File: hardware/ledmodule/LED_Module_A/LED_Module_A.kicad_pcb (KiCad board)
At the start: 2 copper layers, 214.1 x 70.5 mm, 140 parts, among them J1 To MAIN_MOD, U1 DS18B20U

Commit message: Preparation for fabrication
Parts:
- added ?: , LOGO, F.Cu at (249.1, 110.9)
- added H1: MountingHole, MountingHole:MountingHole_3.2mm_M3, F.Cu at (60.0, 125.0)
- added H2: MountingHole, MountingHole:MountingHole_3.2mm_M3, F.Cu at (190.0, 125.0)
- added H3: MountingHole, MountingHole:MountingHole_3.2mm_M3, F.Cu at (250.0, 125.0)
- added H4: MountingHole, MountingHole:MountingHole_3.2mm_M3, F.Cu at (250.0, 87.6)
- added H5: MountingHole, MountingHole:MountingHole_3.2mm_M3, F.Cu at (190.0, 100.0)
- added H6: MountingHole, MountingHole:MountingHole_3.2mm_M3, F.Cu at (85.0, 100.0)
- added H7: MountingHole, MountingHole:MountingHole_3.2mm_M3, F.Cu at (47.4, 88.0)
- D_R1, D_R2, D_R3, D_R4, D_R5, D_R6, D_R7, D_R8: value Photo Red -> Red
- moved D_R5 6.18 mm to (90.0, 104.1)
- moved R_A7 4.64 mm to (79.0, 97.3)
- moved D_A9 2.03 mm to (90.9, 96.5)
- moved D_R7 1.86 mm to (190.5, 106.0)
- moved R_B3 1.68 mm to (212.5, 66.0)
- moved R_B2 1.46 mm to (149.9, 67.5)
- moved D_A4 1.38 mm to (149.9, 72.5)
- moved D_B2 0.46 mm to (96.5, 66.5)
- moved D_P5 0.33 mm to (58.8, 104.1)
- moved R_B1 0.33 mm to (53.9, 100.3)
- moved R_B4 0.33 mm to (53.9, 103.9)
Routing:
- net Net-(D_R5-K): track 2.75 -> 15.1 mm
- net Net-(D_A9-K): track 2.49 -> 10.2 mm
- net Net-(D_P6-K): track 23.2 -> 17.0 mm
- net Net-(D_A8-A): track 20.9 -> 16.1 mm
- net /LED_CW: track 111.8 -> 115.7 mm
- net Net-(D_B5-A): track 20.3 -> 22.5 mm
- net Net-(D_B6-K): track 5.31 -> 3.63 mm
- net Net-(D_W4-K): track 19.3 -> 20.5 mm
- net Net-(D_C10-K): track 19.2 -> 20.2 mm
- net Net-(D_A9-A): track 22.3 -> 21.4 mm
- net Net-(D_P8-K): track 25.7 -> 26.5 mm
- net Net-(D_P7-A): track 25.7 -> 26.5 mm
- net Net-(D_W1-A): track 21.3 -> 22.0 mm
- net Net-(D_W6-K): track 23.8 -> 23.1 mm
- net Net-(D_W5-A): track 3.50 -> 4.24 mm
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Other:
- board size 214.1 x 70.5 mm -> 214.6 x 70.5 mm
- board text added: "J1 (back)"
- board text added: "LED Module A v1.0"
- board text added: "WayWayWay"
- board text added: "https://lenaschimmel.de/besteLampe!"

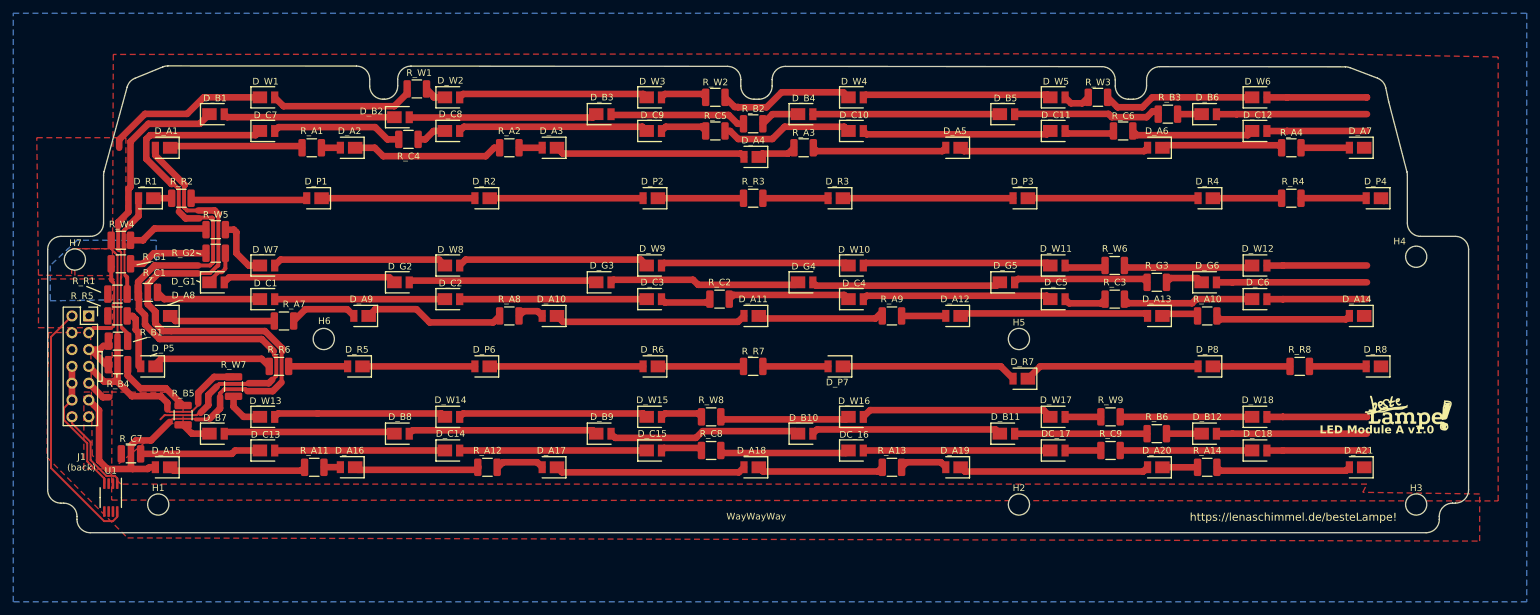
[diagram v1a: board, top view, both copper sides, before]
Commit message: Ready for production - but needs expensive hole plating.
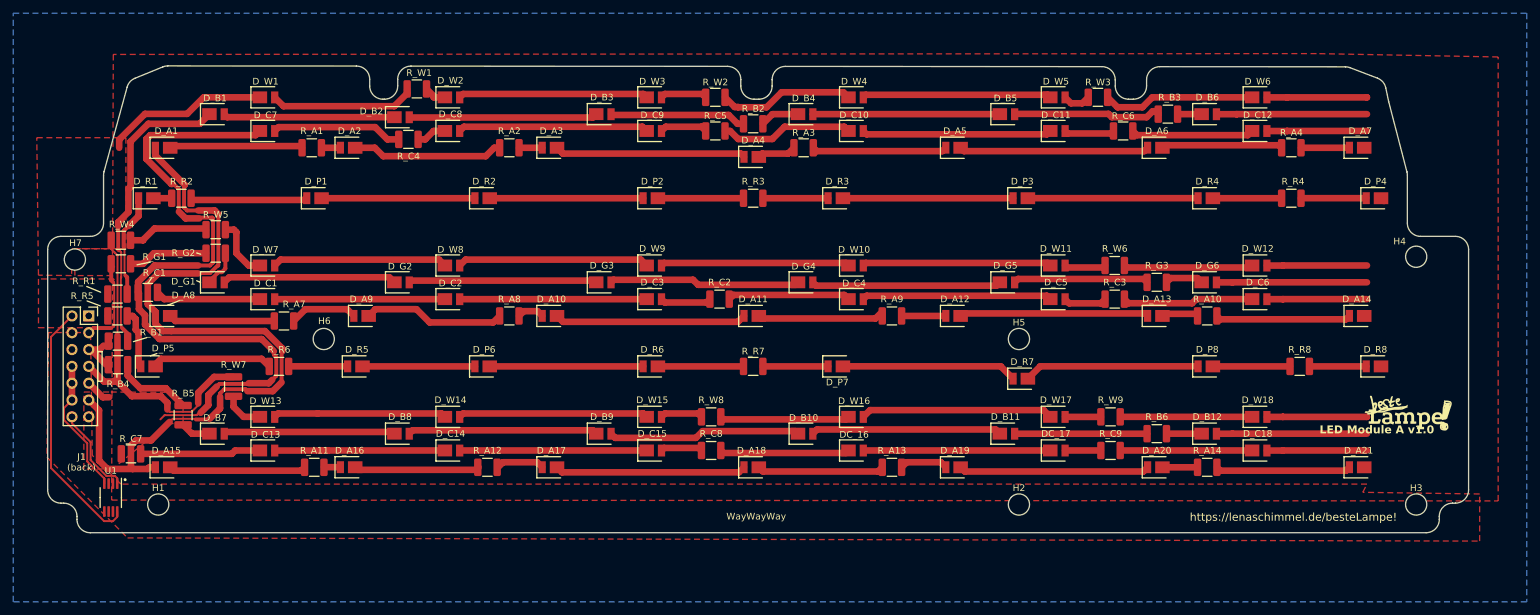
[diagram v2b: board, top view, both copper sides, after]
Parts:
- D_A1, D_A10, D_A11, D_A12, D_A13, D_A14, D_A15, D_A16, D_A17, D_A18, D_A19, D_A2, D_A20, D_A21, D_A3, D_A4, D_A5, D_A6, D_A7, D_A8, D_A9, D_P1, D_P2, D_P3, D_P4, D_P5, D_P6, D_P7, D_P8, D_R1, D_R2, D_R3, D_R4, D_R5, D_R6, D_R7, D_R8: footprint LED_SMD:LED_2835_CREE_JSE28L3E5 -> LED_SMD:LED_2835_CREE_JSE28L3E5_Big_Anode
- J1: value To MAIN_MOD -> Do Not Place
- R_A1, R_A11, R_A7: value 2R2 -> 2.2 Ohm, 0,33W, 5%, 1210 package
- R_A10, R_A12, R_A13, R_A14, R_A2, R_A3, R_A4, R_A8, R_A9, R_C1, R_C2, R_C3, R_C4, R_C5, R_C6, R_C7, R_C8, R_C9, R_G1, R_G2, R_G3, R_W1, R_W2, R_W3, R_W4, R_W5, R_W6, R_W7, R_W8, R_W9: value 18 -> 18 Ohm, 0,5W, 1%, 1210 package
- R_B1, R_B2, R_B3, R_B4, R_B5, R_B6, R_R2, R_R3, R_R4, R_R6, R_R7, R_R8: value 15 -> 15 Ohm, 0,5W, 1%, 1210 package
- R_R1, R_R5: value 4R7 -> 4.7 Ohm, 0,33W, 5%, 1210 package
- U1: value DS18B20U -> DS18B20U+
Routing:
- removed copper zone on B.Cu, net Net-(D_G1-K)

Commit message: SMD pin headers with 90deg rotation
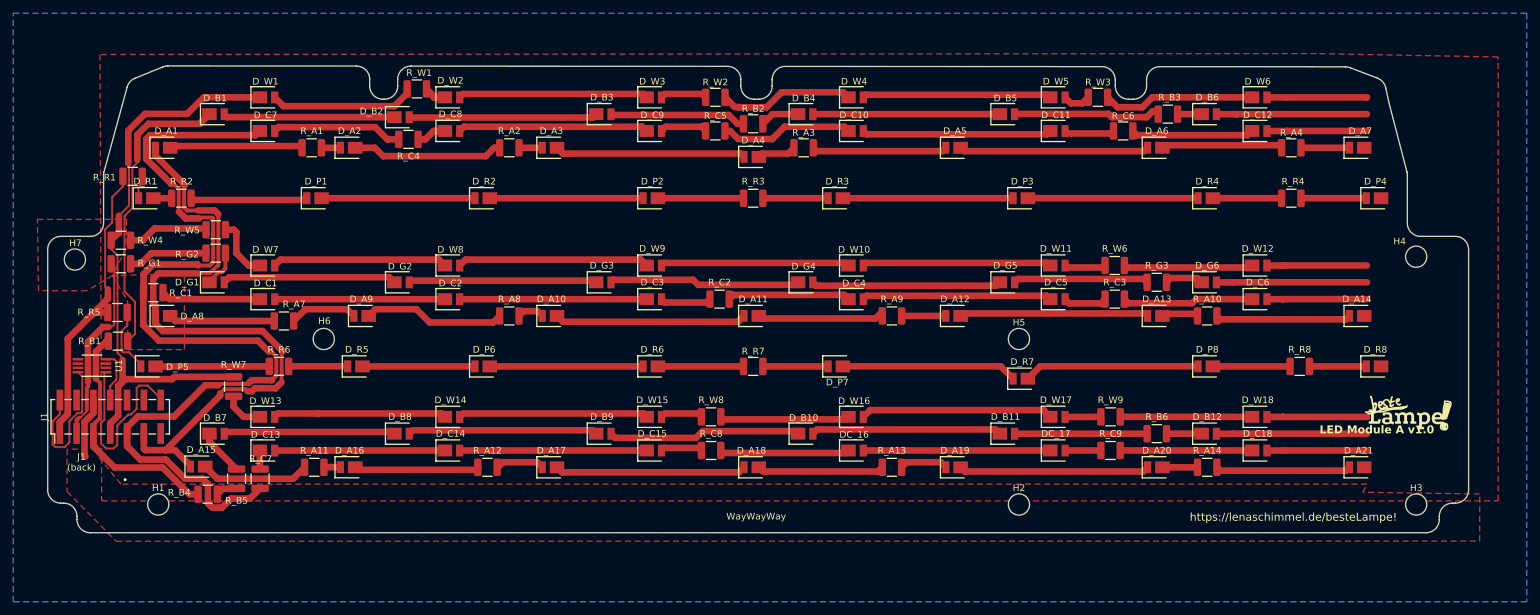
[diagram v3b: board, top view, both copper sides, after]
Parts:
- J1: value Do Not Place -> ~; footprint Connector_PinHeader_2.54mm:PinHeader_2x07_P2.54mm_Vertical_Boxed -> Connector_PinHeader_2.54mm:PinHeader_2x07_P2.54mm_Vertical_SMD; moved to F.Cu
- moved R_B4 23.8 mm to (67.5, 123.4)
- moved U1 20.1 mm to (50.0, 104.0), turned to 180 degrees
- moved R_C7 19.9 mm to (75.4, 121.1), turned to 90 degrees
- moved R_R1 17.9 mm to (56.1, 75.4)
- moved R_B5 12.5 mm to (71.8, 121.1), turned to 90 degrees
- moved J1 8.84 mm to (52.8, 111.8), turned to 90 degrees
- moved D_A15 5.28 mm to (66.2, 119.3)
- moved R_C1 0.83 mm to (59.2, 93.0)
- moved R_R5 0.52 mm to (53.8, 96.0)
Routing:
- net /LED_R: track 0.01 -> 45.9 mm
- net /LED_CW: track 115.7 -> 146.7 mm
- net /LED_B: track 6.06 -> 35.8 mm
- net /LED_A: track 120.8 -> 102.0 mm
- net +3V3: track 38.7 -> 22.1 mm
- net /LED_G: track 14.3 -> 30.3 mm
- net Net-(D_R1-K): track 18.1 -> 2.66 mm
- net Net-(D_C13-K): track 18.2 -> 2.82 mm
- net /TEMP: track 13.7 -> 28.9 mm
- net /LED_WW: track 76.8 -> 90.4 mm
- net GND: track 20.7 -> 7.94 mm
- net +24V: track 159.6 -> 170.0 mm
- net Net-(R_B4-Pad2): track 11.9 -> 3.27 mm
- net Net-(D_A15-A): track 20.7 -> 16.6 mm
- net Net-(D_B7-K): track 4.53 -> 7.49 mm
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- removed copper zone on F.Cu, net /LED_CW
- removed copper zone on F.Cu, net /LED_G

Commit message: New layout with angled SMD header, but probably not aligned correctly.
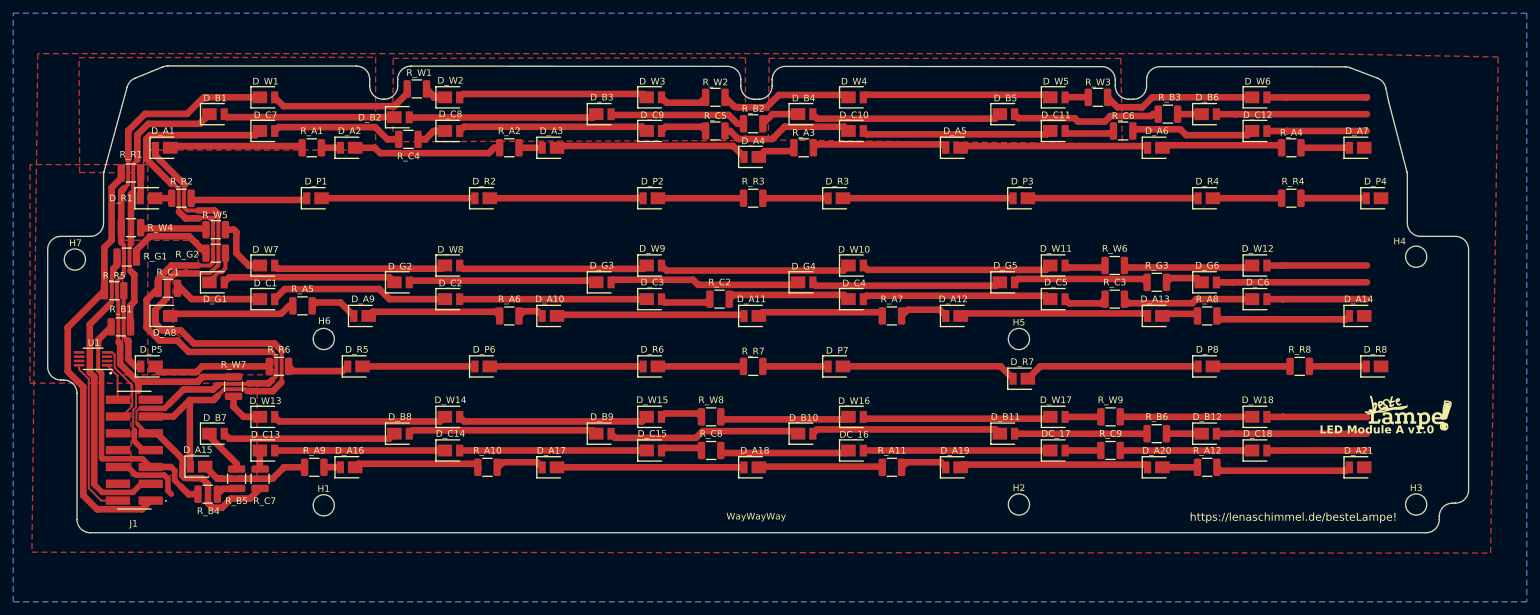
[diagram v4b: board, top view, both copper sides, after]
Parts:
- J1: footprint Connector_PinHeader_2.54mm:PinHeader_2x07_P2.54mm_Vertical_SMD -> TSM:TSM-107-YY-ZZZ-DV-P-TR
- moved H1 25.0 mm to (85.0, 125.1)
- moved J1 6.22 mm to (56.4, 116.8), turned to -90 degrees
- moved R_A5 3.61 mm to (81.8, 95.0)
- moved R_R5 3.33 mm to (53.3, 92.7)
- moved R_W4 2.44 mm to (55.9, 83.2)
- moved R_C1 2.29 mm to (61.5, 92.3)
- moved R_B1 2.20 mm to (54.4, 98.2)
- moved R_G1 1.35 mm to (55.2, 87.6)
- moved U1 1.06 mm to (50.2, 103.0)
- moved R_R1 0.57 mm to (55.9, 74.9)
- moved D_R1 0.25 mm to (58.7, 78.7), turned to 0 degrees
- turned D_A1 to 0 degrees
- turned D_A10 to 0 degrees
- turned D_A11 to 0 degrees
- turned D_A12 to 0 degrees
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- renumbered R_A12 to R_A10, R_A13 to R_A11, R_A14 to R_A12, R_A7 to R_A5, R_A8 to R_A6, R_A9 to R_A7, R_A10 to R_A8, R_A11 to R_A9
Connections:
- J1 pad 10: GND -> unconnected-(J1-Pin_10-Pad10)
- J1 pad 8: GND -> unconnected-(J1-Pin_8-Pad8)
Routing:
- net /TEMP: track 28.9 -> 5.85 mm
- net /LED_R: track 45.9 -> 64.6 mm
- net /LED_G: track 30.3 -> 47.2 mm
- net /LED_B: track 35.8 -> 43.1 mm
- net Net-(D_R5-K): track 15.1 -> 9.51 mm
- net GND: track 7.94 -> 12.9 mm
- net /LED_CW: track 146.7 -> 141.8 mm
- net /LED_A: track 102.0 -> 97.8 mm
- net /LED_WW: track 90.4 -> 94.4 mm
- net Net-(D_A8-A): track 16.1 -> 19.2 mm
- net Net-(D_B1-K): track 45.3 -> 42.2 mm
- net Net-(D_P5-K): track 10.2 -> 13.2 mm
- net Net-(D_A9-K): track 10.2 -> 7.34 mm
- net Net-(R_W4-Pad2): track 12.2 -> 10.0 mm
- net +3V3: track 22.1 -> 24.3 mm
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- added copper zone on F.Cu, net /LED_A
- added copper zone on F.Cu, net /LED_CW
- added copper zone on F.Cu, net Net-(D_W2-A)
- added copper zone on F.Cu, net Net-(D_W4-A)
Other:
- outline, holes or cut-outs redrawn
- board text removed: "J1 (back)"

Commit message: And yet another connector. This one should be perfect!
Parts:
- J1: footprint TSM:TSM-107-YY-ZZZ-DV-P-TR -> Pin Header Wuerth:610114249121
- moved J1 5.20 mm to (51.3, 118.0)
- moved U1 0.89 mm to (50.2, 102.1)
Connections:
- J1 pad 1: /LED_R -> +3V3
- J1 pad 10: unconnected-(J1-Pin_10-Pad10) -> /LED_CW
- J1 pad 11: /LED_A -> GND
- J1 pad 12: GND -> /LED_A
- J1 pad 13: /NEO -> /TEMP
- J1 pad 14: /TEMP -> /NEO
- J1 pad 2: +3V3 -> /LED_R
- J1 pad 3: /LED_G -> +5V
- J1 pad 4: +5V -> /LED_G
- J1 pad 5: /LED_B -> +24V
- J1 pad 6: +24V -> /LED_B
- J1 pad 7: /LED_WW -> unconnected-(J1-Pad7)
- J1 pad 8: unconnected-(J1-Pin_8-Pad8) -> /LED_WW
- J1 pad 9: /LED_CW -> unconnected-(J1-Pad9)
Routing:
- net /LED_B: track 43.1 -> 37.9 mm
- net +3V3: track 24.3 -> 27.5 mm
- net /TEMP: track 5.85 -> 8.78 mm
- net GND: track 12.9 -> 15.6 mm
- net +24V: track 171.8 -> 169.5 mm
- net /LED_CW: track 141.8 -> 139.7 mm
- net /LED_WW: track 94.4 -> 92.3 mm
- net /LED_A: track 97.8 -> 96.0 mm
- net /LED_R: track 64.6 -> 66.1 mm
- net /LED_G: track 47.2 -> 46.7 mm
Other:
- outline, holes or cut-outs redrawn

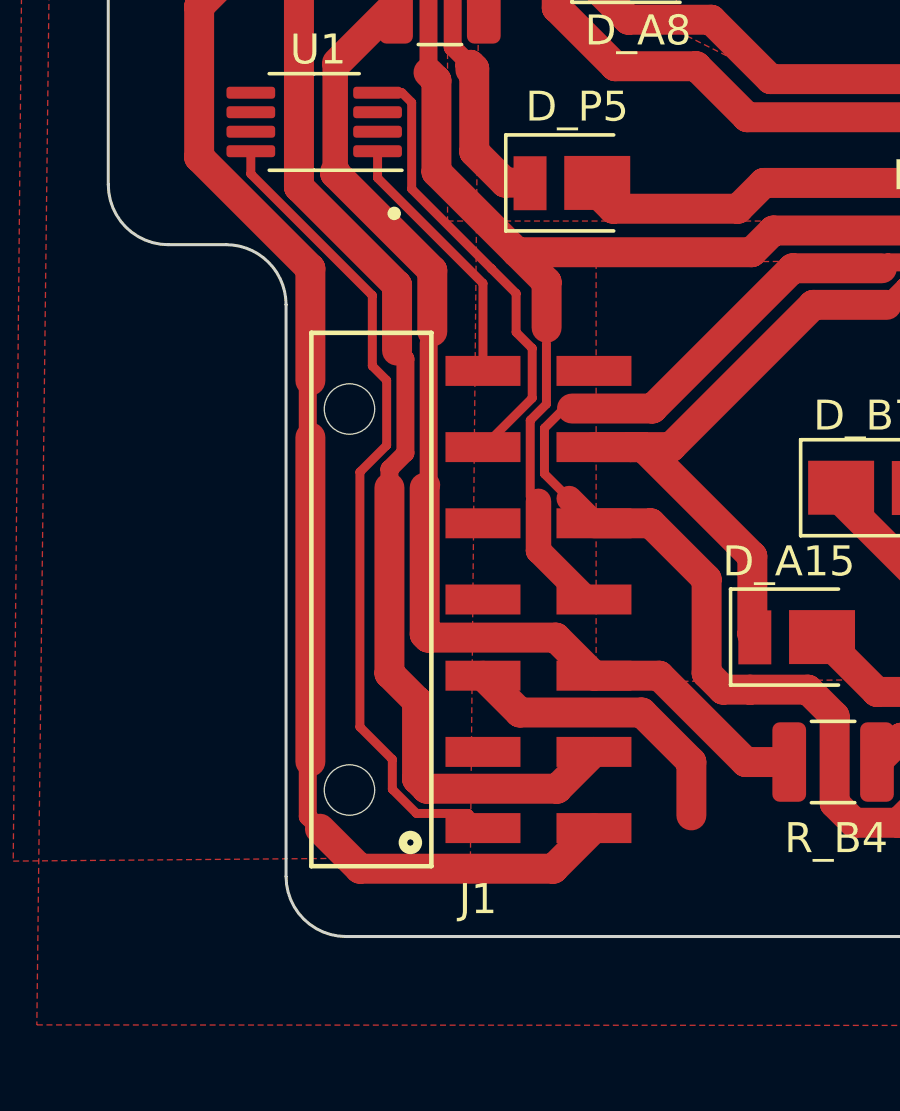
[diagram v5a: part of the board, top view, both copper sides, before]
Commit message: Exchange out-of-stock LEDs by alternatives, clean up parts table.
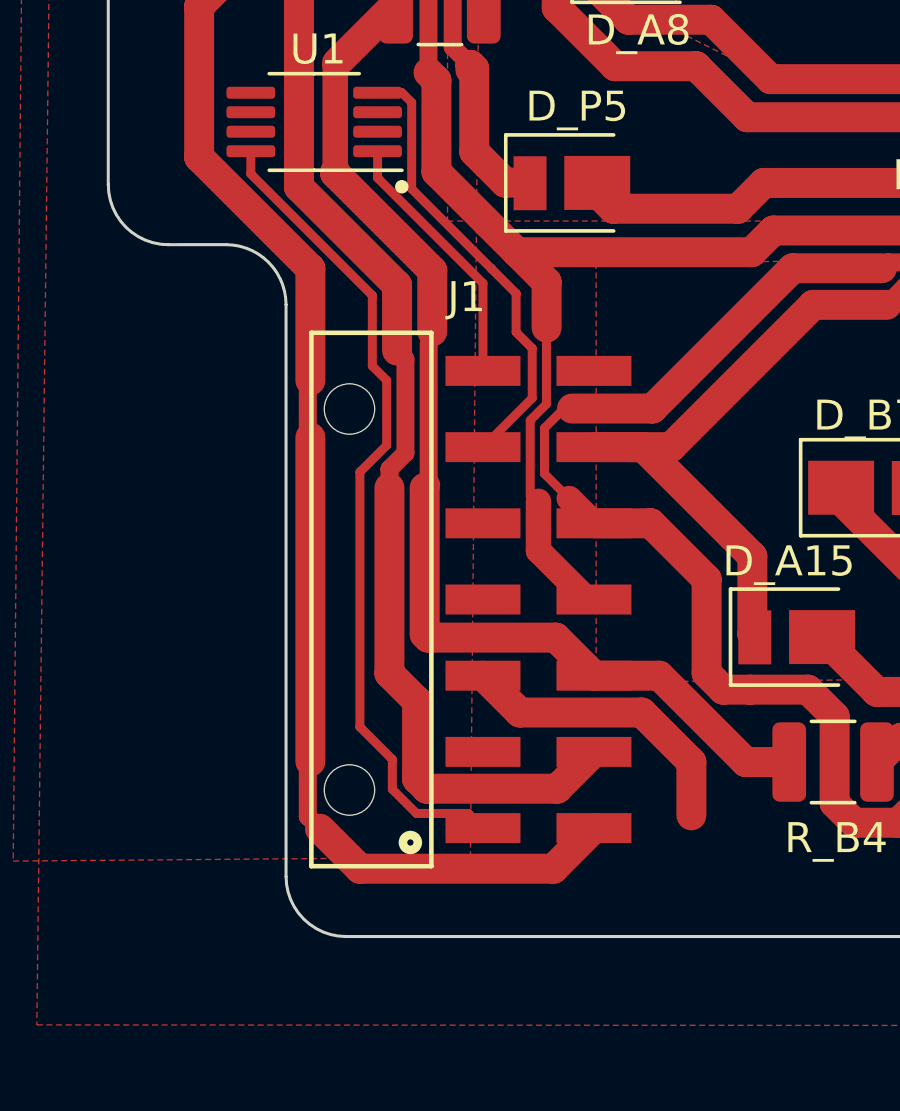
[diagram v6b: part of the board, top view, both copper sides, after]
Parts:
- D_B1, D_B10, D_B11, D_B12, D_B2, D_B3, D_B4, D_B5, D_B6, D_B7, D_B8, D_B9: value Blue -> Royal Blue
- J1: value ~ -> Connector Header Surface Mount, Right Angle 14 position 0.100 (2.54mm)
- R_A1, R_A5, R_A9: value 2.2 Ohm, 0,33W, 5%, 1210 package -> 2.2 Ohm, 0.33W, 5%, 1210 package
- R_A10, R_A11, R_A12, R_A2, R_A3, R_A4, R_A6, R_A7, R_A8, R_C1, R_C2, R_C3, R_C4, R_C5, R_C6, R_C7, R_C8, R_C9, R_G1, R_G2, R_G3, R_W1, R_W2, R_W3, R_W4, R_W5, R_W6, R_W7, R_W8, R_W9: value 18 Ohm, 0,5W, 1%, 1210 package -> 18 Ohm, 0.5W, 1%, 1210 package
- R_B1, R_B2, R_B3, R_B4, R_B5, R_B6, R_R2, R_R3, R_R4, R_R6, R_R7, R_R8: value 15 Ohm, 0,5W, 1%, 1210 package -> 15 Ohm, 0.5W, 1%, 1210 package
- R_R1, R_R5: value 4.7 Ohm, 0,33W, 5%, 1210 package -> 4.7 Ohm, 0.33W, 5%, 1210 package
